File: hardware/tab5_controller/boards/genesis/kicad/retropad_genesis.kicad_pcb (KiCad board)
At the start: 2 copper layers, 125 x 55 mm, 38 parts, among them J1 Tab5 Ext.Port1, J2 SWD, SW1 UP, SW2 DOWN, SW3 LEFT, SW4 RIGHT, SW5 A, SW6 B, SW7 C, SW8 START, SW9 MENU, U1 STM32F030C8T6

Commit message: tab5_controller: redesign Genesis board as the 6-button pad
X Y Z now sit in a row above A B C (14 mm columns, rising 1.5 mm per
column, rows 16.5 mm apart), with MODE beside START on the SELECT bit and
MENU above. The board is re-routed: 0 unconnected pads, no DRC errors
beyond silkscreen warnings, schematic vs PCB 0 differences, and button
wiring and ID straps verified.

layout.py now also checks footprint courtyards and the M3 holes'
courtyards. The first 6-button attempt passed the pad checks but DRC
found overlapping courtyards; the four existing boards pass the new
check unchanged.

The Genesis core (gwenesis) still emulates only the 3-button pad, so
X/Y/Z/MODE are reported by the board but ignored until the core and the
host map gain 6-button support; documented in genesis/README.md.

Co-Authored-By: Claude Opus 5.5 <noreply@anthropic.com>
Claude-Session: https://claude.ai/code/session_01NhSHTsezreiVZCnuBhQzP2
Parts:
- added D10: 1N4148W, Diode_SMD:D_SOD-123, B.Cu at (152.0, 107.0)
- added D11: 1N4148W, Diode_SMD:D_SOD-123, B.Cu at (97.8, 119.0)
- added D12: 1N4148W, Diode_SMD:D_SOD-123, B.Cu at (110.2, 119.0)
- added D13: 1N4148W, Diode_SMD:D_SOD-123, B.Cu at (104.0, 109.0)
- added SW10: Z, Button_Switch_THT:SW_PUSH-12mm, F.Cu at (149.5, 113.2)
- added SW11: MODE, Button_Switch_THT:SW_PUSH_6mm, F.Cu at (93.9, 119.7)
- added SW12: START, Button_Switch_THT:SW_PUSH_6mm, F.Cu at (106.3, 119.7)
- added SW13: MENU, Button_Switch_THT:SW_PUSH_6mm, F.Cu at (100.1, 109.7)
- SW6: value B -> X
- SW7: value C -> B
- SW8: value START -> Y; footprint Button_Switch_THT:SW_PUSH_6mm -> Button_Switch_THT:SW_PUSH-12mm
- SW9: value MENU -> C; footprint Button_Switch_THT:SW_PUSH_6mm -> Button_Switch_THT:SW_PUSH-12mm
- moved SW9 53.3 mm to (149.5, 129.8), turned to 90 degrees
- moved D9 50.2 mm to (152.0, 123.5), turned to 90 degrees
- moved D8 36.4 mm to (138.0, 108.5), turned to 90 degrees
- moved SW8 36.2 mm to (135.5, 114.8), turned to 90 degrees
- moved D7 19.8 mm to (138.0, 125.0)
- moved SW7 19.8 mm to (135.5, 131.2)
- moved D6 14.6 mm to (124.0, 110.0)
- moved SW6 14.6 mm to (121.5, 116.2)
- moved D5 9.50 mm to (124.0, 126.5)
- moved SW5 9.50 mm to (121.5, 132.8)
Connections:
- net K_START renamed K_Y
- D6 pad 1: K_B -> K_X
- D6 pad 2: ROW5 -> ROW7
- D7 pad 1: K_C -> K_B
- D7 pad 2: ROW6 -> ROW5
- D8 pad 2: ROW6 -> ROW0
- D9 pad 1: K_MENU -> K_C
- D9 pad 2: ROW0 -> ROW6
- SW6 pad 1: K_B -> K_X
- SW7 pad 1: K_C -> K_B
- SW9 pad 1: K_MENU -> K_C
- SW9 pad 2: COL2 -> COL0
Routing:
- net COL1: track 33.5 -> 120.0 mm, vias 0 -> 1
- net ROW7: track 0.00 -> 77.2 mm, vias 0 -> 3
- net ROW1: track 54.7 -> 100.4 mm, vias 0 -> 3
- net ROW0: track 47.4 -> 82.2 mm
- net +3V3: track 162.0 -> 127.6 mm
- net SDA: track 38.8 -> 70.0 mm, vias 2 -> 0
- net ROW4: track 38.2 -> 56.1 mm, vias 2 -> 0
- net K_Z: track 0.00 -> 14.6 mm
- net K_X: track 0.00 -> 14.6 mm
- net ROW5: track 46.6 -> 60.0 mm
- net NRST: track 49.0 -> 35.9 mm, vias 0 -> 2
- net ROW6: track 100.2 -> 113.2 mm
- net K_START: track 0.00 -> 9.84 mm
- net K_MODE: track 0.00 -> 9.84 mm
- net COL0: track 206.6 -> 215.6 mm, vias 0 -> 1
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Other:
- board text added: "RetroPad Genesis / Mega Drive 6-button (console ID 5)"
- board text removed: "RetroPad Genesis / Mega Drive (console ID 5)"

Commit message: tab5_controller: build every console board on the AVR32DD28
The STM32F030 matrix boards are gone. SNES, NES, Game Boy, Genesis and
Master System / Game Gear are now all AVR32DD28 boards: one MCU pin per
button, no diodes, UPDI programming, one firmware image (firmware_avrdd)
keyed by the console-ID straps.

- layout.py / gen_pcb.py / gen_sch.py: drop the stm32 core (LQFP-48,
  key matrix, diodes, SWD header, AN_EN strap); the AVR DD core is the
  only one, and the *_dd board names become the plain console names.
- SNES, NES and Genesis keep the routing of their AVR DD prototypes;
  Game Boy and Master System are routed fresh.
- Every board: DRC 0 unconnected (silkscreen warnings only), schematic
  vs PCB 0 differences, and each switch checked against the MCU pin
  pinmap.h gives it for that console ID.
- Host test now also covers the Game Boy and Master System pin maps.
- READMEs describe the AVR DD boards only.

Co-Authored-By: Claude Opus 5.5 <noreply@anthropic.com>
Claude-Session: https://claude.ai/code/session_01NhSHTsezreiVZCnuBhQzP2
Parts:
- removed C5: 100nF, Capacitor_SMD:C_0603_1608Metric
- removed D1, D10, D11, D12, D13, D2, D3, D4, D5, D6, D7, D8, D9: 1N4148W, Diode_SMD:D_SOD-123
- removed R10: DNP, Resistor_SMD:R_0603_1608Metric
- removed R4, R5: 10k, Resistor_SMD:R_0603_1608Metric
- added R11: DNP, Resistor_SMD:R_0603_1608Metric, B.Cu at (76.0, 93.0)
- J2: value SWD -> UPDI; footprint Connector_PinHeader_2.54mm:PinHeader_1x05_P2.54mm_Vertical -> Connector_PinHeader_2.54mm:PinHeader_1x03_P2.54mm_Vertical
- U1: value STM32F030C8T6 -> AVR32DD28-I/SO; footprint Package_QFP:LQFP-48_7x7mm_P0.5mm -> Package_SO:SOIC-28W_7.5x17.9mm_P1.27mm
- moved R3 17.2 mm to (97.6, 85.7)
- moved C4 12.7 mm to (116.0, 90.5), turned to 90 degrees
- moved C2 11.5 mm to (102.1, 85.7)
- moved C3 7.98 mm to (106.0, 101.6), turned to 180 degrees
- moved C1 5.83 mm to (92.0, 96.0)
- moved J2 2.00 mm to (130.0, 86.5)
- moved R6 2.00 mm to (121.0, 99.0)
- moved R7 2.00 mm to (124.0, 99.0)
- moved R8 2.00 mm to (127.0, 99.0)
- moved R9 2.00 mm to (130.0, 99.0)
- moved U1 0.50 mm to (104.0, 93.5), turned to 90 degrees
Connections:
- J1 pad 10: (no net) -> G9_UPDI
- J1 pad 9: INT -> (no net)
- J2 pad 2: SWCLK -> UPDI
- J2 pad 3: SWDIO -> GND
- R3 pad 2: INT -> RESET
- SW1 pad 2: COL0 -> GND
- SW10 pad 2: COL1 -> GND
- SW11 pad 2: COL1 -> GND
- SW12 pad 2: COL1 -> GND
- SW13 pad 2: COL2 -> GND
- SW2 pad 2: COL0 -> GND
- SW3 pad 2: COL0 -> GND
- SW4 pad 2: COL0 -> GND
- SW5 pad 2: COL0 -> GND
- SW6 pad 2: COL0 -> GND
- SW7 pad 2: COL0 -> GND
- SW8 pad 2: COL1 -> GND
- SW9 pad 2: COL0 -> GND
- U1 pad 1: +3V3 -> ID3
- U1 pad 10: COL0 -> K_RIGHT
- U1 pad 11: COL1 -> K_A
- U1 pad 12: COL2 -> K_X
- U1 pad 13: COL3 -> K_B
- U1 pad 14: (no net) -> +3V3
- U1 pad 15: (no net) -> GND
- U1 pad 16: (no net) -> K_START
- U1 pad 17: (no net) -> K_MENU
- U1 pad 18: ROW0 -> RESET
- U1 pad 19: ROW1 -> UPDI
- U1 pad 2: (no net) -> K_Y
- U1 pad 20: ROW2 -> +3V3
- U1 pad 21: SCL -> GND
- U1 pad 22: SDA -> ID0
- U1 pad 23: GND -> ID1
- U1 pad 24: +3V3 -> SDA
- U1 pad 25: ID0 -> SCL
- U1 pad 26: ID1 -> AN0
- U1 pad 27: ID2 -> AN1
- U1 pad 28: (no net) -> ID2
- U1 pad 3: (no net) -> K_C
- U1 pad 4: (no net) -> K_Z
- U1 pad 5: (no net) -> K_MODE
- U1 pad 6: (no net) -> +3V3
- U1 pad 7: NRST -> K_UP
- U1 pad 8: GND -> K_DOWN
- U1 pad 9: +3V3 -> K_LEFT
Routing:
- net GND: track 131.7 -> 368.4 mm, vias 3 -> 2
- net COL0: track 215.6 -> 0.00 mm, vias 1 -> 0
- net COL1: track 120.0 -> 0.00 mm, vias 1 -> 0
- net ROW6: track 113.2 -> 0.00 mm
- net ROW1: track 100.4 -> 0.00 mm, vias 3 -> 0
- net ROW0: track 82.2 -> 0.00 mm, vias 2 -> 0
- net ROW7: track 77.2 -> 0.00 mm, vias 3 -> 0
- net K_C: track 14.6 -> 80.3 mm
- net UPDI: track 0.00 -> 64.1 mm, vias 0 -> 1
- net ROW5: track 60.0 -> 0.00 mm, vias 2 -> 0
- net ROW2: track 58.4 -> 0.00 mm
- net ROW4: track 56.1 -> 0.00 mm
- net K_B: track 14.6 -> 61.7 mm, vias 0 -> 1
- net K_LEFT: track 9.41 -> 54.9 mm
- net INT: track 44.0 -> 0.00 mm, vias 1 -> 0
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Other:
- board text added: "ID0 ID1 ID2 ID3"
- board text added: "UPDI 3V3 UPDI GND"
- board text removed: "ID0 ID1 ID2 ID3 AN"
- board text removed: "SWD 3V3 CLK DIO RST GND"

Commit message: tab5_controller: remove the UPDI-to-G9 link (R11) from every board
The Tab5 never updates controller firmware, so J1 pin 10 (G9) is left
unconnected, as on M5Stack's keyboard, and R11 and the G9_UPDI net are
gone. Boards are programmed only through their own UPDI header J2.

All five boards are re-routed (the old routes ended at R11). Game Boy
is routed with Freerouting 2.1 single-threaded because 1.9 stalls with
UPDI unrouted on it. Every board: DRC 0 unconnected pads (silkscreen
warnings only), schematic vs PCB 0 differences, switches on the pins
pinmap.h expects.

Co-Authored-By: Claude Opus 5.5 <noreply@anthropic.com>
Claude-Session: https://claude.ai/code/session_01NhSHTsezreiVZCnuBhQzP2
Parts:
- removed R11: DNP, Resistor_SMD:R_0603_1608Metric
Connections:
- J1 pad 10: G9_UPDI -> (no net)
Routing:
- net UPDI: track 64.1 -> 28.5 mm
- net K_C: track 80.3 -> 63.0 mm
- net G9_UPDI: track 7.36 -> 0.00 mm
- net +3V3: track 104.7 -> 110.1 mm
- net GND: track 368.4 -> 364.7 mm
- net SCL: track 63.8 -> 65.9 mm
- net RESET: track 6.31 -> 4.78 mm
- net SDA: track 62.8 -> 63.9 mm
- net K_MENU: track 26.0 -> 27.0 mm, vias 2 -> 1
- net K_START: track 38.8 -> 39.0 mm, vias 2 -> 1

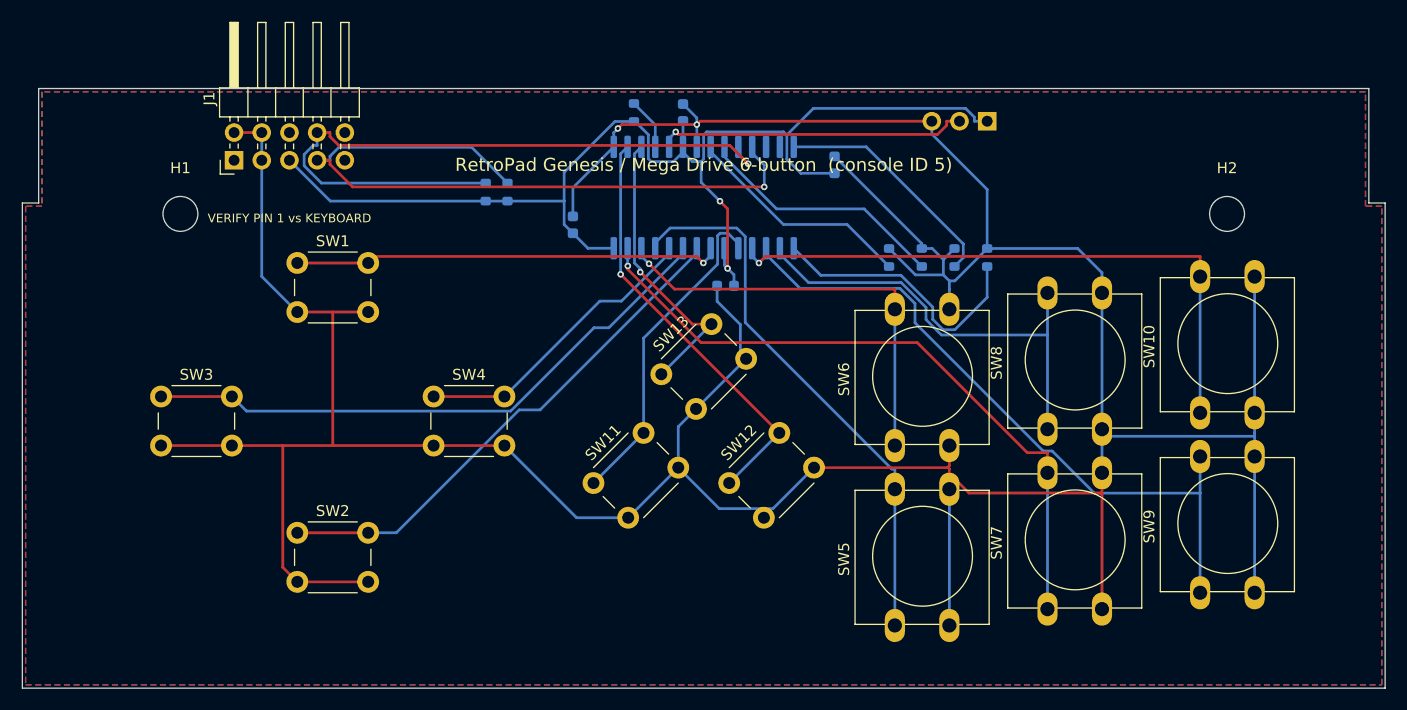
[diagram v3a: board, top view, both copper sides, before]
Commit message: tab5_controller: 0805 hand-solder passives on every board
Swap the 0603 resistors and capacitors (decoupling, I2C pull-ups, reset
pull-up, console-ID straps) for KiCad's 0805 HandSolder footprints, which
have longer pads for soldering by hand. C2 turns 90 degrees so its larger
courtyard clears U1. All four boards are re-routed with Freerouting 1.9;
schematics, BOMs, DRC reports and renders are regenerated.

DRC: 0 errors and 0 unconnected pads on every board (silkscreen and
library-path warnings only). Schematic vs PCB: 0 differences.

Co-Authored-By: Claude Opus 5.5 <noreply@anthropic.com>
Claude-Session: https://claude.ai/code/session_016pgTnJvu7Wh4anaUwDfFmN
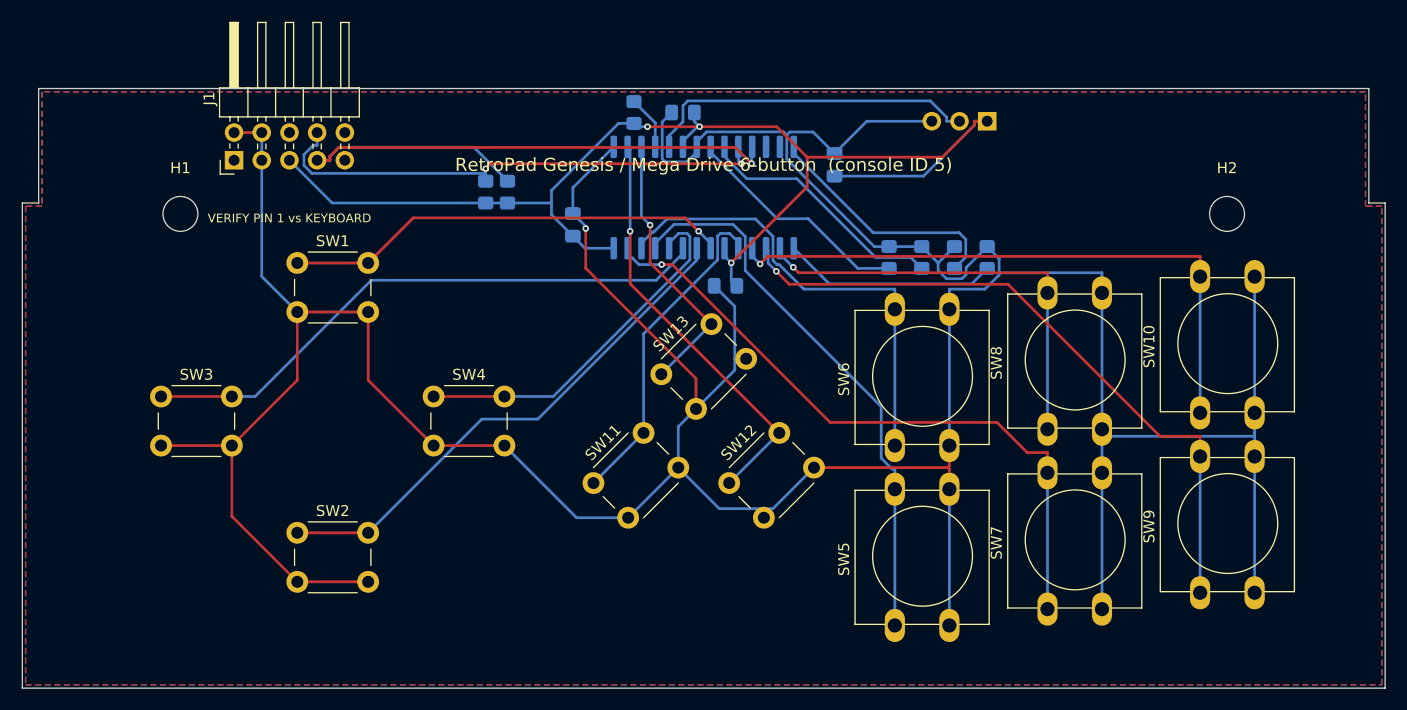
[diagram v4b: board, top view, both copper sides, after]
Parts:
- C1, C2, C3, C4: footprint Capacitor_SMD:C_0603_1608Metric -> Capacitor_SMD:C_0805_2012Metric_Pad1.18x1.45mm_HandSolder
- R1, R2, R3, R6, R7, R8, R9: footprint Resistor_SMD:R_0603_1608Metric -> Resistor_SMD:R_0805_2012Metric_Pad1.20x1.40mm_HandSolder
- turned C2 to 180 degrees
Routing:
- net SDA: track 63.9 -> 47.2 mm, vias 1 -> 2
- net GND: track 364.7 -> 376.1 mm, vias 2 -> 1
- net +3V3: track 110.1 -> 117.1 mm, vias 2 -> 3
- net K_RIGHT: track 27.5 -> 33.7 mm
- net ID3: track 25.6 -> 19.7 mm
- net SCL: track 65.9 -> 62.2 mm
- net K_X: track 39.6 -> 42.9 mm, vias 1 -> 0
- net UPDI: track 28.5 -> 30.8 mm, vias 1 -> 0
- net K_UP: track 39.4 -> 41.0 mm
- net K_MENU: track 27.0 -> 25.4 mm
- net K_Y: track 41.3 -> 40.1 mm, vias 0 -> 1
- net K_LEFT: track 54.9 -> 53.8 mm
- net ID2: track 21.6 -> 22.7 mm
- net K_C: track 63.0 -> 62.0 mm, vias 0 -> 1
- net K_B: track 61.8 -> 60.9 mm
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
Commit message: tab5_controller: 4-pin tact switch symbols and footprints
The 6x6 and 12x12 switches are 4-leg parts, and the production layout in
EasyEDA uses their 4-pin symbols, so the KiCad boards now match:

- kicad_lib/RetroPad.pretty: SW_PUSH_6mm_4pin and SW_PUSH-12mm_4pin,
  KiCad's footprints with the pads renumbered 1-4 (pad 1 top-left, then
  clockwise; tied pairs 1-2 and 3-4, the legs 6.5 / 12.5 mm apart).
  gen_pcb.py writes them from the stock footprints and points each
  board's fp-lib-table at the library.
- RetroPad:SW_Push_4pin symbol in gen_sch.py: 1-2 tied, 4-3 tied, one
  contact between. KiCad's 4-pin SW_Push_Dual is a two-contact switch,
  so it doesn't fit these parts.
- Wiring: legs 1-2 to GND, 3-4 to K_<button>. L/R (right angle, two
  contacts plus mounting legs) keep the 2-pin SW_Push.
- All four boards re-routed: DRC 0 unconnected (silkscreen warnings
  only), schematic vs PCB 0 differences, every switch on the pin
  pinmap.h expects; firmware host test passes; Gerber/drill export OK.

Co-Authored-By: Claude Opus 5.5 <noreply@anthropic.com>
Claude-Session: https://claude.ai/code/session_01NhSHTsezreiVZCnuBhQzP2
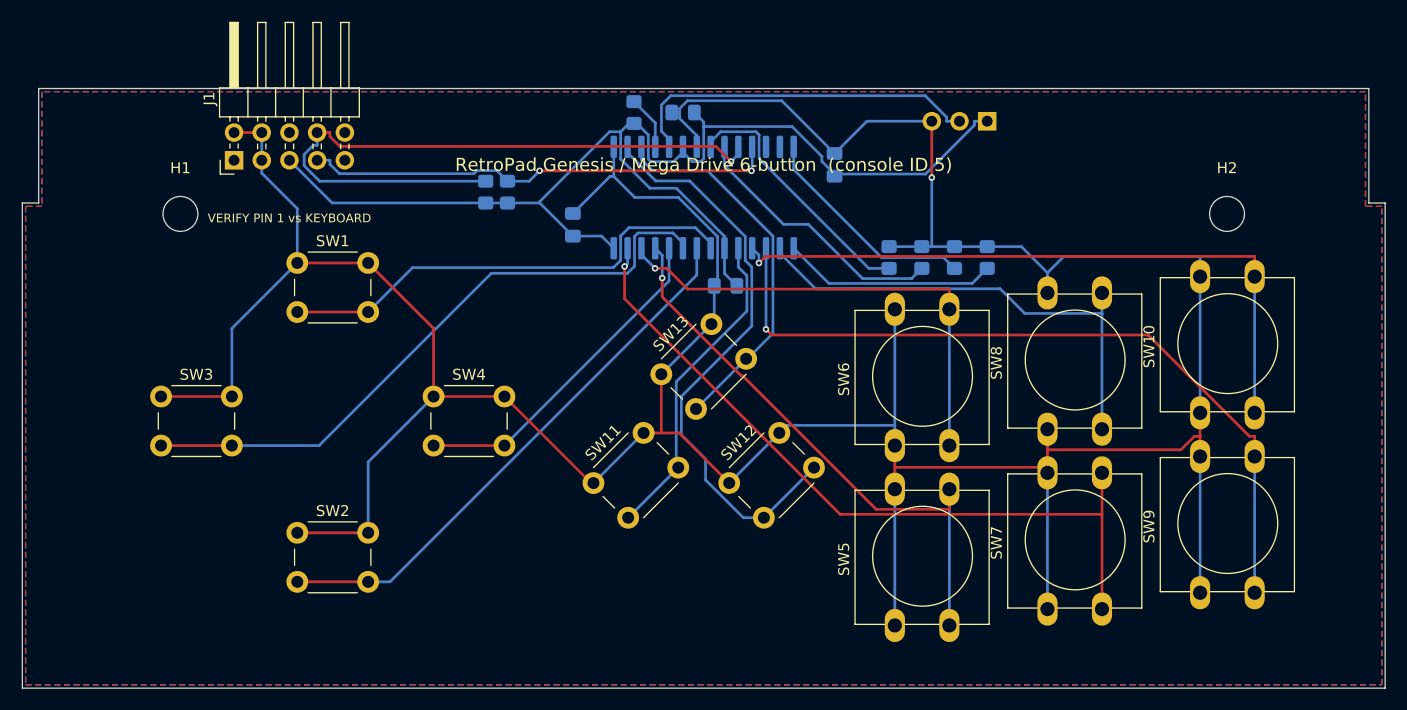
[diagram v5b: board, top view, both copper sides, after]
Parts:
- SW1, SW11, SW12, SW13, SW2, SW3, SW4: footprint Button_Switch_THT:SW_PUSH_6mm -> RetroPad:SW_PUSH_6mm_4pin
- SW10, SW5, SW6, SW7, SW8, SW9: footprint Button_Switch_THT:SW_PUSH-12mm -> RetroPad:SW_PUSH-12mm_4pin
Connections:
- SW1 pad 1: K_UP -> GND
- SW10 pad 1: K_Z -> GND
- SW11 pad 1: K_MODE -> GND
- SW12 pad 1: K_START -> GND
- SW13 pad 1: K_MENU -> GND
- SW2 pad 1: K_DOWN -> GND
- SW3 pad 1: K_LEFT -> GND
- SW4 pad 1: K_RIGHT -> GND
- SW5 pad 1: K_A -> GND
- SW6 pad 1: K_X -> GND
- SW7 pad 1: K_B -> GND
- SW8 pad 1: K_Y -> GND
- SW9 pad 1: K_C -> GND
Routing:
- net GND: track 376.1 -> 351.1 mm
- net SCL: track 62.2 -> 43.7 mm, vias 1 -> 2
- net K_START: track 38.5 -> 54.0 mm, vias 1 -> 0
- net SDA: track 47.2 -> 61.9 mm, vias 2 -> 1
- net K_MENU: track 25.4 -> 35.0 mm, vias 1 -> 0
- net K_C: track 62.0 -> 70.7 mm
- net K_B: track 60.9 -> 69.2 mm
- net +3V3: track 117.1 -> 110.4 mm, vias 3 -> 0
- net K_Z: track 56.7 -> 61.7 mm
- net K_Y: track 40.1 -> 44.8 mm, vias 1 -> 0
- net K_LEFT: track 53.8 -> 58.4 mm
- net K_RIGHT: track 33.7 -> 30.9 mm
- net K_DOWN: track 48.1 -> 50.8 mm
- net K_UP: track 41.0 -> 43.5 mm, vias 1 -> 0
- net ID0: track 21.3 -> 23.7 mm
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
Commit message: tab5_controller: label each console-ID strap under its own resistor
The back silkscreen printed one mirrored "ID0 ID1 ID2 ID3" string, which
reads left to right from the back while the straps appear right to left
(R9/ID3 first), so the labels were in the reverse order of the parts.
Each strap now gets its own ID<n> label centred under it. Silkscreen
only: the boards keep their routing (same segments and vias), DRC 0
unconnected, schematic vs PCB 0 differences.

Co-Authored-By: Claude Opus 5.5 <noreply@anthropic.com>
Claude-Session: https://claude.ai/code/session_01NhSHTsezreiVZCnuBhQzP2
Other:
- board text added: "ID0"
- board text added: "ID1"
- board text added: "ID2"
- board text added: "ID3"
- board text removed: "ID0 ID1 ID2 ID3"
